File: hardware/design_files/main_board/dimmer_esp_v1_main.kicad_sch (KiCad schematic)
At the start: 43 parts, among them IC1 PEC11S-929K-S0015, J1 SM05B-SRSS-TB_LF__SN_, J3 USB_C_Receptacle, J4 Conn_01x02, J5 Conn_01x02, J6 Conn_01x02, J7 Conn_01x04, J8 Screw_Terminal_01x03, K2 FINDER-34.51, SW1 Commission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

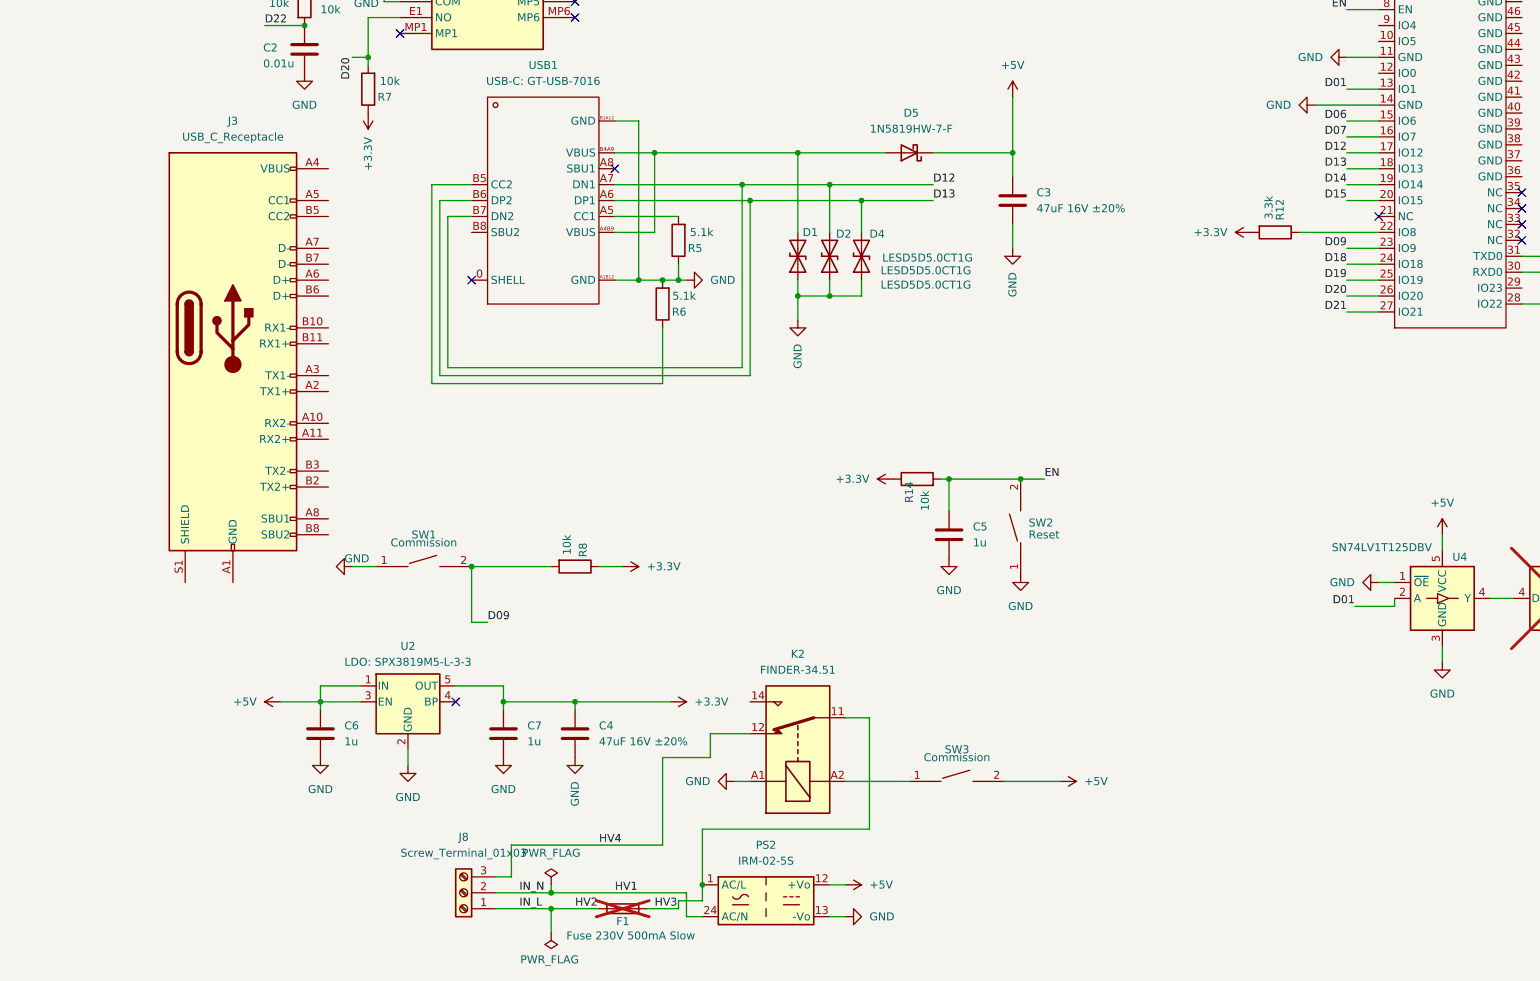
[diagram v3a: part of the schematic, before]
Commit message: Add toggle circuit, arrange components on PCB
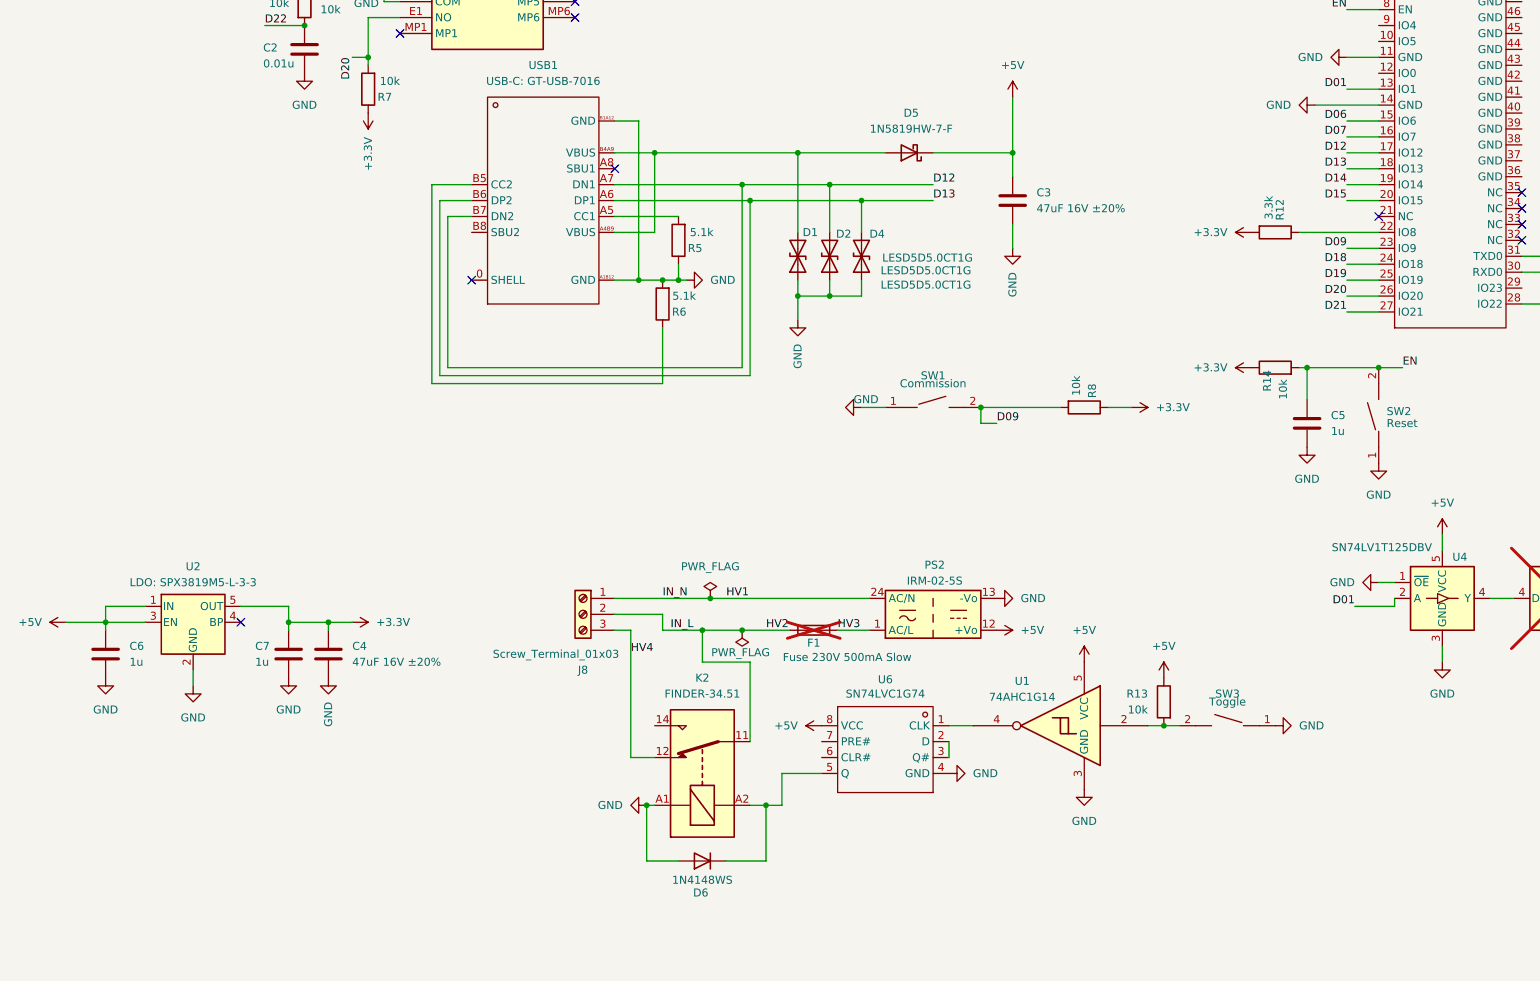
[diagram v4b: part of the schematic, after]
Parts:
- removed J3: USB_C_Receptacle, Connector_USB:USB_C_Receptacle_JAE_DX07S024WJ3R400, symbol Connector:USB_C_Receptacle
- added D6: 1N4148WS, Diode_SMD:D_SOD-323, symbol Diode:1N4148WS
- added R13: 10k, Resistor_SMD:R_0603_1608Metric, symbol Device:R
- added U1: 74AHC1G14, Package_TO_SOT_SMD:SOT-353_SC-70-5, symbol 74xGxx:74AHC1G14
- added U6: SN74LVC1G74, Package_SO:VSSOP-8_2.3x2mm_P0.5mm, symbol 74xx:SN74LVC1G74DCUR_C70285
- SW3: value Commission -> Toggle
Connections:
- net +5V: now also R13.1, U1.5 (VCC), U6.8 (VCC); no longer SW3.2
- net GND: now also SW3.1, D6.2 (A), U1.3 (GND), U6.4 (GND)
- net HV1: now also J8.1 (Pin_1); no longer J8.2 (Pin_2)
- net HV2: now also J8.2 (Pin_2), K2.11; no longer J8.1 (Pin_1)
- net HV3: no longer K2.11
- net at K2.A2: now also D6.1 (K), U6.5 (Q); no longer SW3.1
- new net: R13.2, SW3.2, U1.2
- new net: U1.4, U6.1 (CLK)
- new net: U6.2 (D), U6.3 (Q#)
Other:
- moved on the sheet: C4, C5, C6, C7, F1, J8, K2, PS2, R14, R8, SW1, SW2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

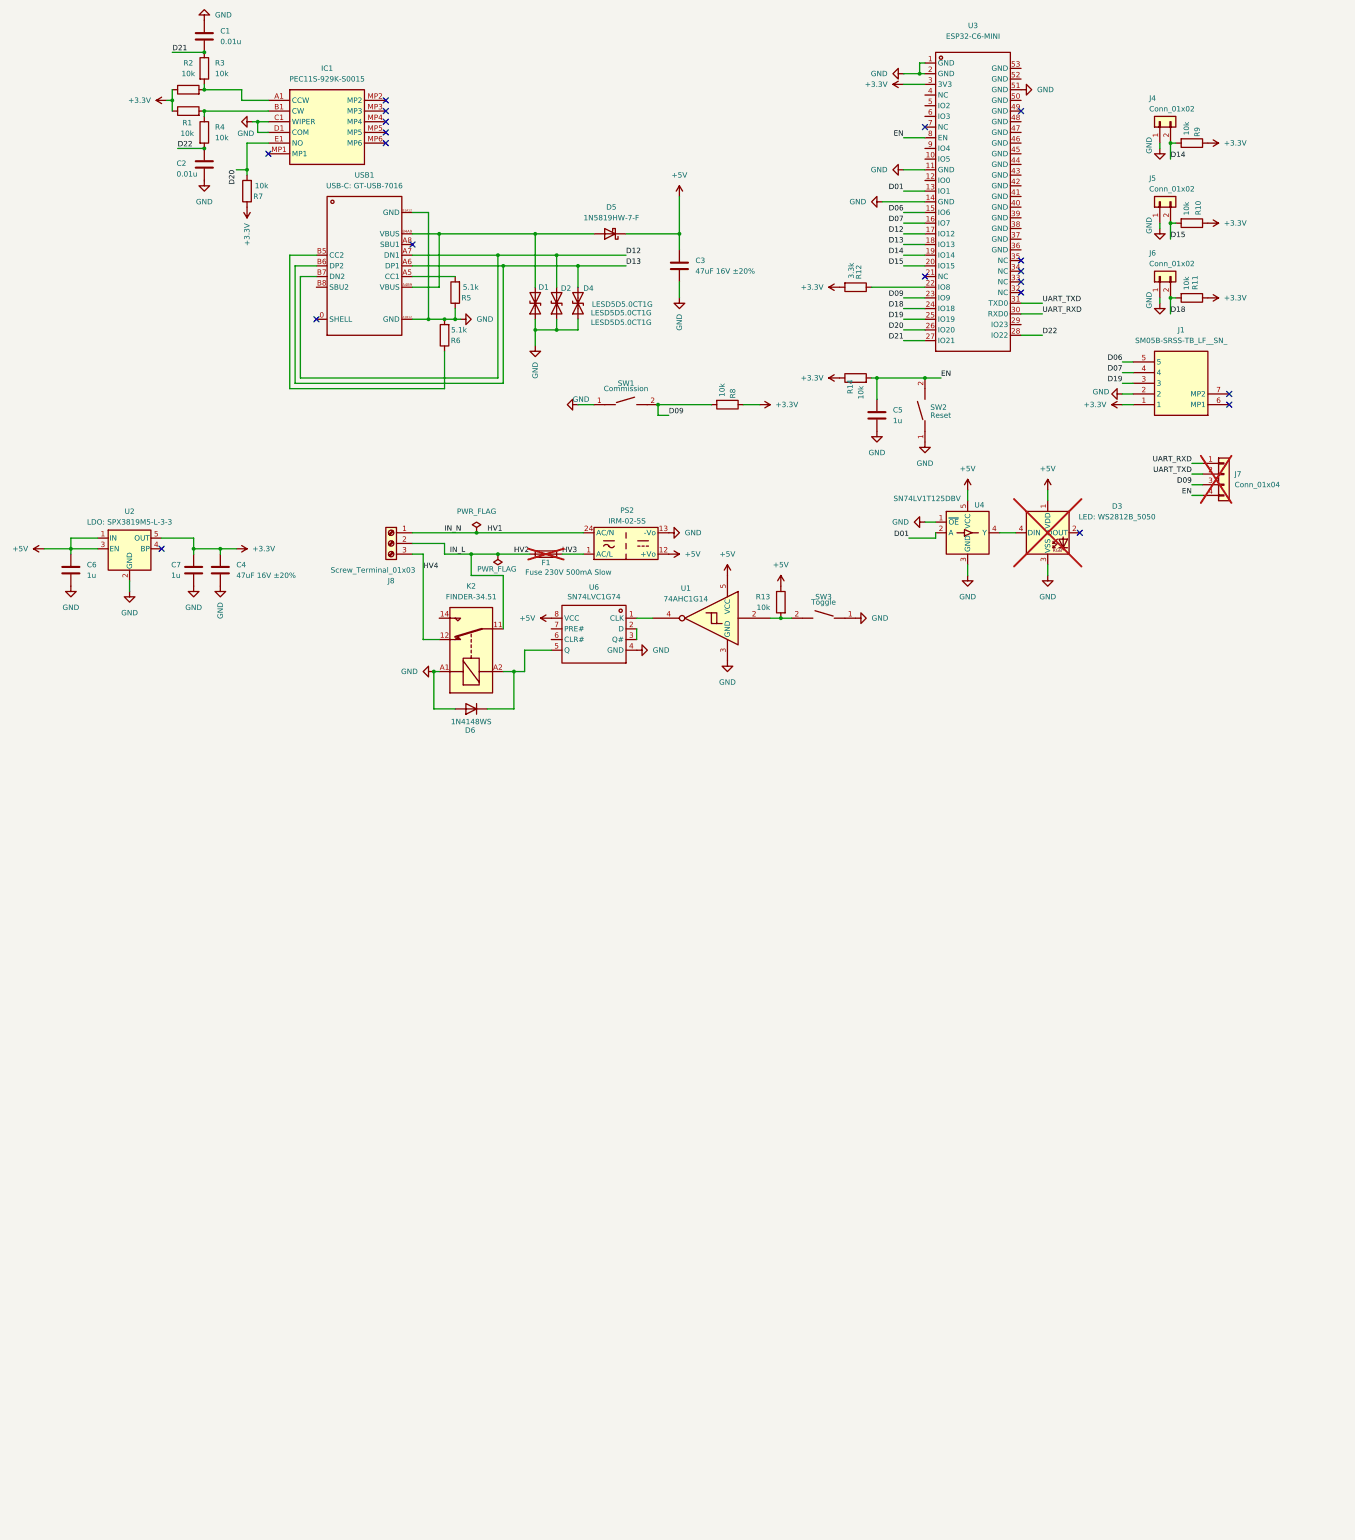
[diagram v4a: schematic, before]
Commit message: Add circuit for external encoder
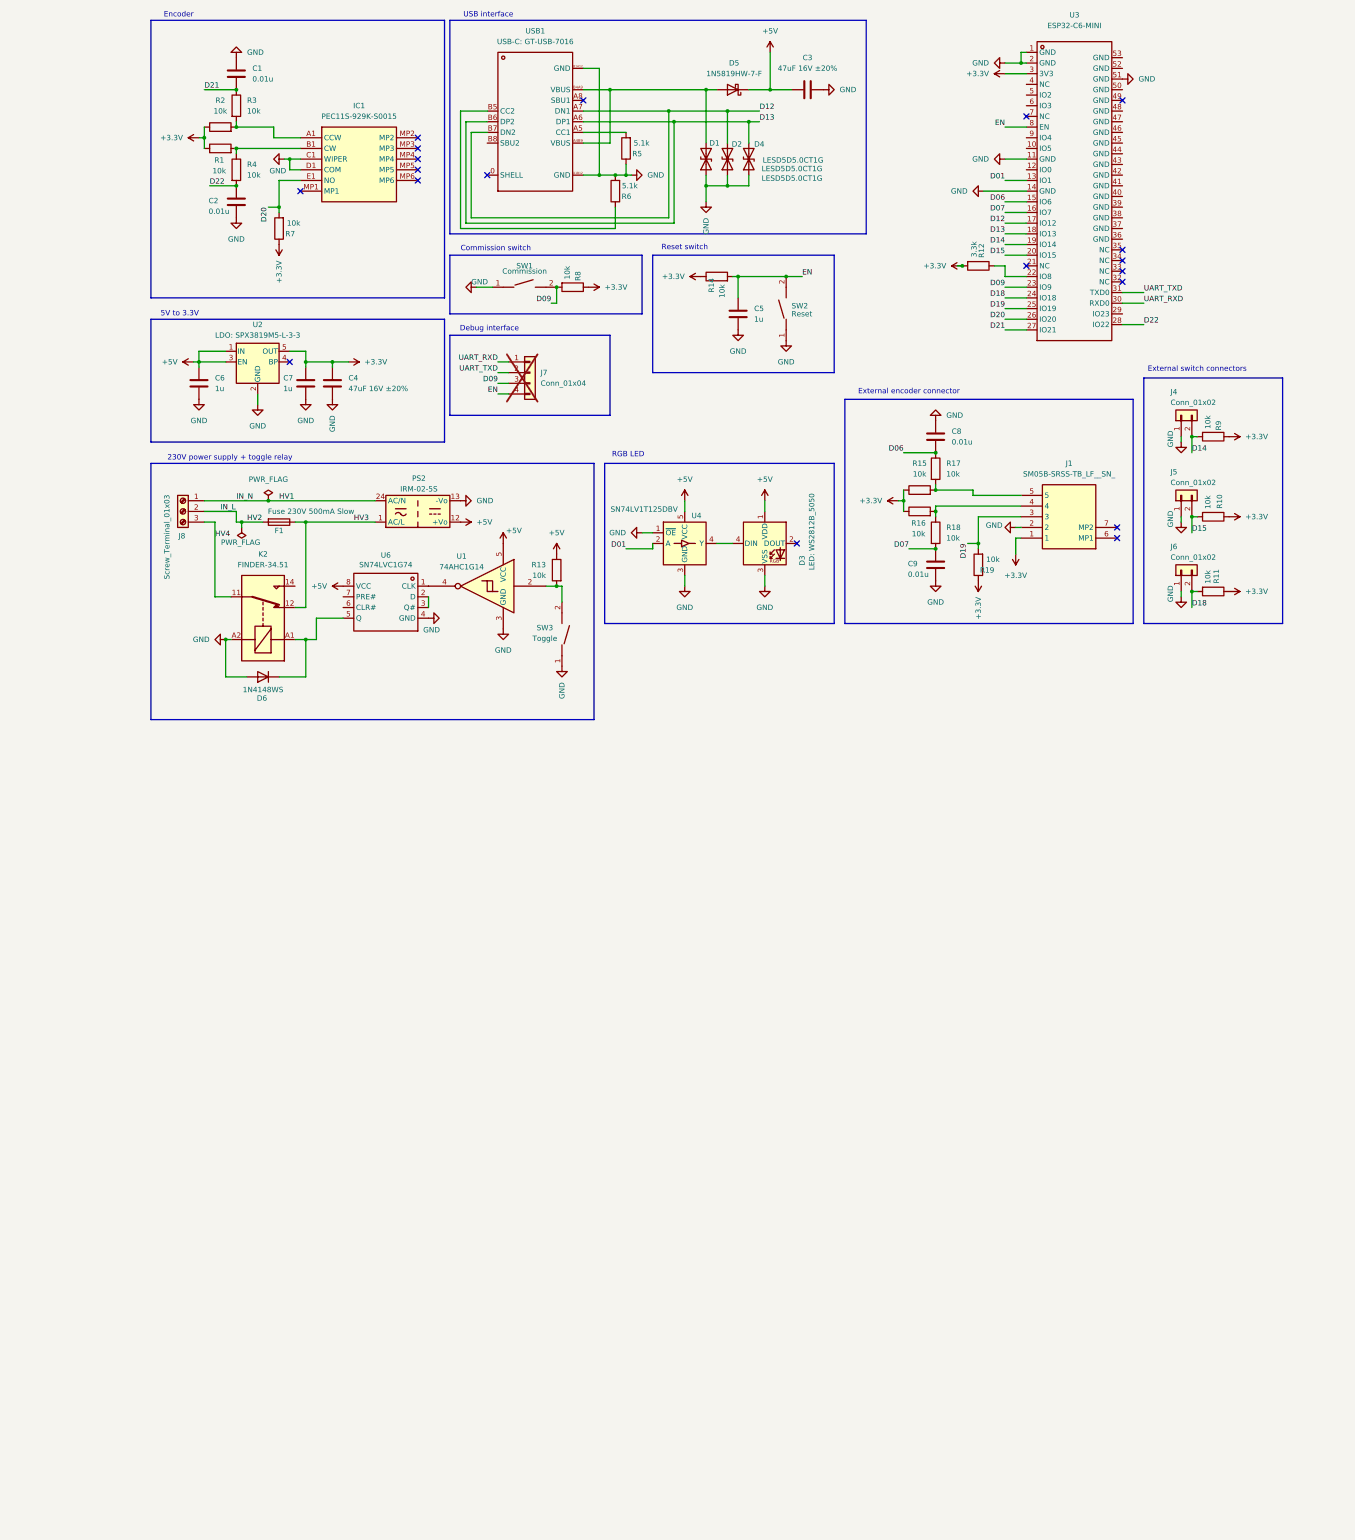
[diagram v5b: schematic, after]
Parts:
- added C8, C9: 0.01u, Capacitor_SMD:C_0603_1608Metric, symbol Device:C
- added R15, R16, R17, R18, R19: 10k, Resistor_SMD:R_0603_1608Metric, symbol Device:R
- D3, F1: now fitted
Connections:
- net +3.3V: now also R15.1, R16.1, R19.1
- net D06: now also C8.2, R17.1; no longer J1.5
- net D07: now also C9.2, R18.2; no longer J1.4
- net D19: now also R19.2
- net GND: now also K2.A2, C8.1, C9.1; no longer K2.A1
- net HV2: no longer K2.11
- net HV3: now also K2.12
- net HV4: now also K2.11; no longer K2.12
- net at D6.1 (K), U6.5 (Q): now also K2.A1; no longer K2.A2
- new net: J1.4, R16.2, R18.1
- new net: J1.5, R15.2, R17.2
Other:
- note added: "230V power supply + toggle relay"
- note added: "5V to 3.3V"
- note added: "Commission switch"
- note added: "Debug interface"
- note added: "Encoder"
- note added: "External encoder connector"
- note added: "External switch connectors"
- note added: "RGB LED"
- note added: "Reset switch"
- note added: "USB interface"
- moved on the sheet: C1, C2, C3, C4, C5, C6, C7, D1, D2, D4, D5, D6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

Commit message: Add correct relay
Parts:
- removed K2: FINDER-34.51, Relay_THT:Relay_SPDT_Finder_34.51_Vertical, symbol Relay:FINDER-34.51
- added K1: FTR-LYCA005Y, FTRLYCA024Y, symbol relay_mouser:FTR-LYCA005Y
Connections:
- net GND: now also K1.1 (COIL_1)
- net HV3: now also K1.3 (NC)
- net HV4: now also K1.4 (COM)
- net at D6.1 (K), U6.5 (Q): now also K1.2 (COIL_2)
- no-connect marks 19 -> 22
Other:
- moved on the sheet: D6

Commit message: Add correct USB, fix button layout
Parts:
- removed USB1: USB-C: GT-USB-7016, usb_jlc:USB-C-SMD_GT-USB-7016B, symbol ProProject_New Project_2024-06-28_12-44-45_2024-06-28:GT-USB-7016
- added USB2: USB-TYPE-C-018, usb_jlc:USB-C_SMD-TYPE-C-31-M-12, symbol usb_jlc:USB-TYPE-C-018
- C1, C2, C8, C9: LCSC C15195 -> C57112
- C3, C4: footprint Capacitor_SMD:C_Elec_4x5.4 -> Capacitor_SMD:C_Elec_5x5.4
- D3: LCSC (none) -> C2843785
- D6: LCSC (none) -> C2128
- F1: LCSC (none) -> C315874
- IC1: LCSC (none) -> C5362681
- J8: LCSC (none) -> C480520
- K1: footprint FTRLYCA024Y -> relay_mouser:FTRLYCA024Y; now not fitted
- PS2: LCSC (none) -> C7211217
- R1, R10, R11, R14, R15, R16, R17, R18, R19, R2, R3, R4, R7, R8, R9: LCSC C1523 -> C25804
- R13: LCSC (none) -> C25804
- SW1, SW2, SW3: LCSC (none) -> C720477
- U1: LCSC (none) -> C460491
- U4: value SN74LV1T125DBV -> SN74LV1T125DBVR
- U6: value SN74LVC1G74 -> SN74LVC1G74DCUR; LCSC (none) -> C70285
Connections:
- net D12: now also USB2.A7 (DN1), USB2.B7 (DN2)
- net D13: now also USB2.A6 (DP1), USB2.B6 (DP2)
- net GND: now also USB2.A1 (GND), USB2.A12 (GND), USB2.B1 (GND), USB2.B12 (GND)
- net at D1.2 (A2), D5.2 (A): now also USB2.A4 (VBUS), USB2.A9 (VBUS), USB2.B4 (VBUS), USB2.B9 (VBUS)
- net at R5.2: now also USB2.A5 (CC1)
- net at R6.1: now also USB2.B5 (CC2)
- no-connect marks 22 -> 26
